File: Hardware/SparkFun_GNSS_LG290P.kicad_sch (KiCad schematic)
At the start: 59 parts, among them J1 USB_C_Receptacle, J10 Conn_01x06, J2 Conn_01x06, J3 SMA_Edge, J4 Qwiic_RA, J5 SMA_Edge, J6 Conn_01x09, J7 Qwiic_RA, J8 JST_Locking_4, J9 I2C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

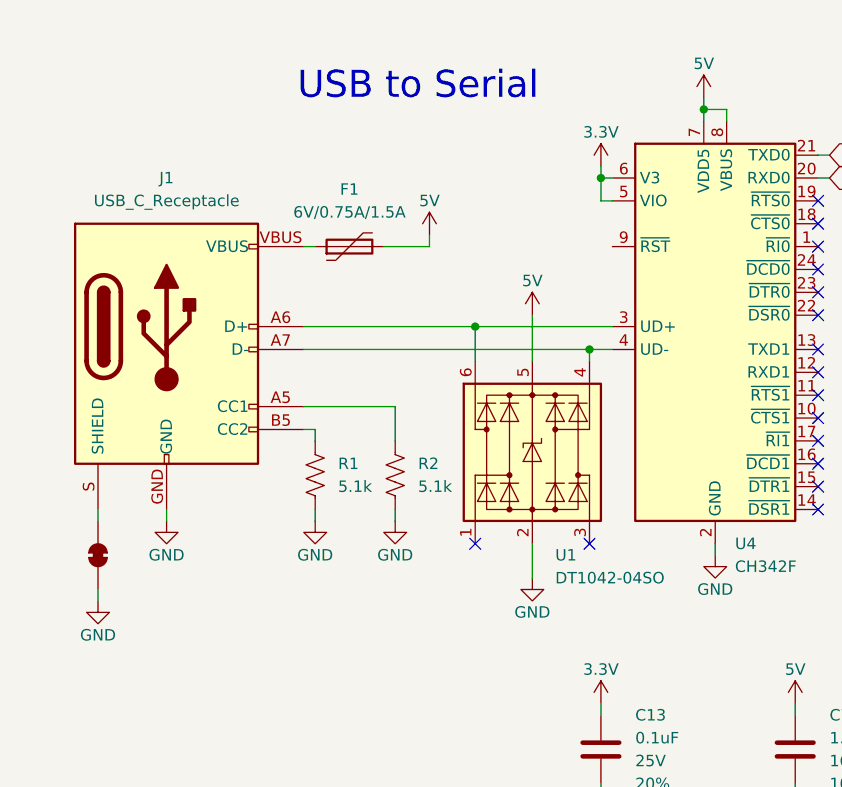
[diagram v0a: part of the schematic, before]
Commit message: Connect CH342 V3 to decoupling cap
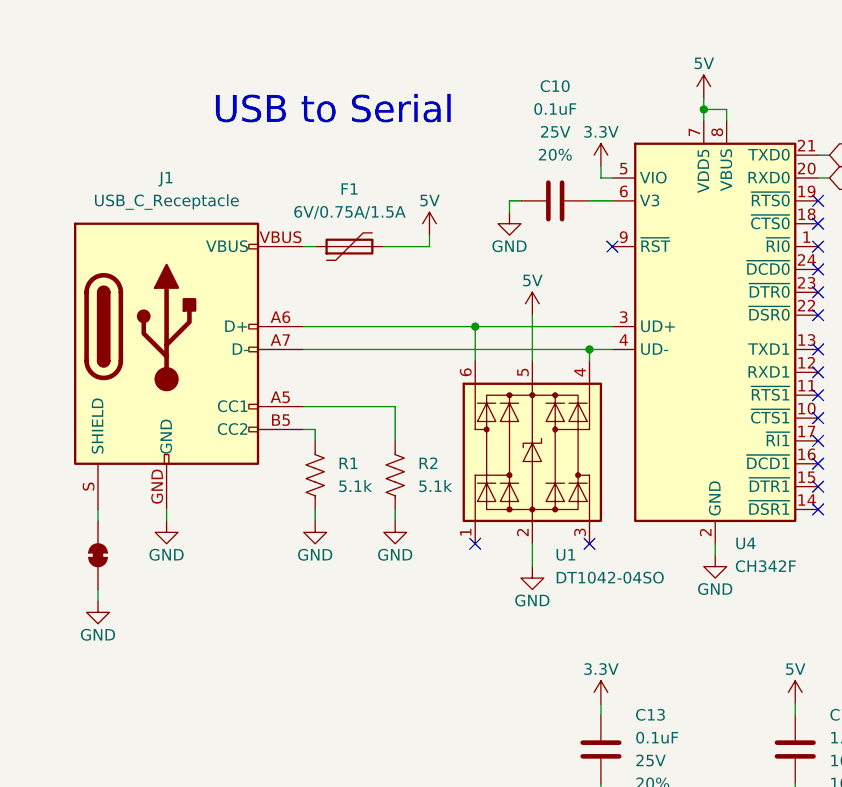
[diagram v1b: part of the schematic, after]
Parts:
- added C10: 0.1uF, SparkFun-Capacitor:C_0603_1608Metric, symbol SparkFun-Capacitor:0.1uF_0603_25V_20%
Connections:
- net 3.3V: no longer U4.6 (V3)
- net GND: now also C10.1
- net at J4.NC1 (NC): no longer J4.NC2 (NC)
- net at J1.NC2 (NC): no longer J1.NC3 (NC)
- net at J7.NC1 (NC): no longer J7.NC2 (NC)
- new net: C10.2, U4.6 (V3)
- now unconnected: U3.1 (NC), U3.17 (NC), U3.2 (NC), U3.5 (NC)
- no-connect marks 19 -> 20

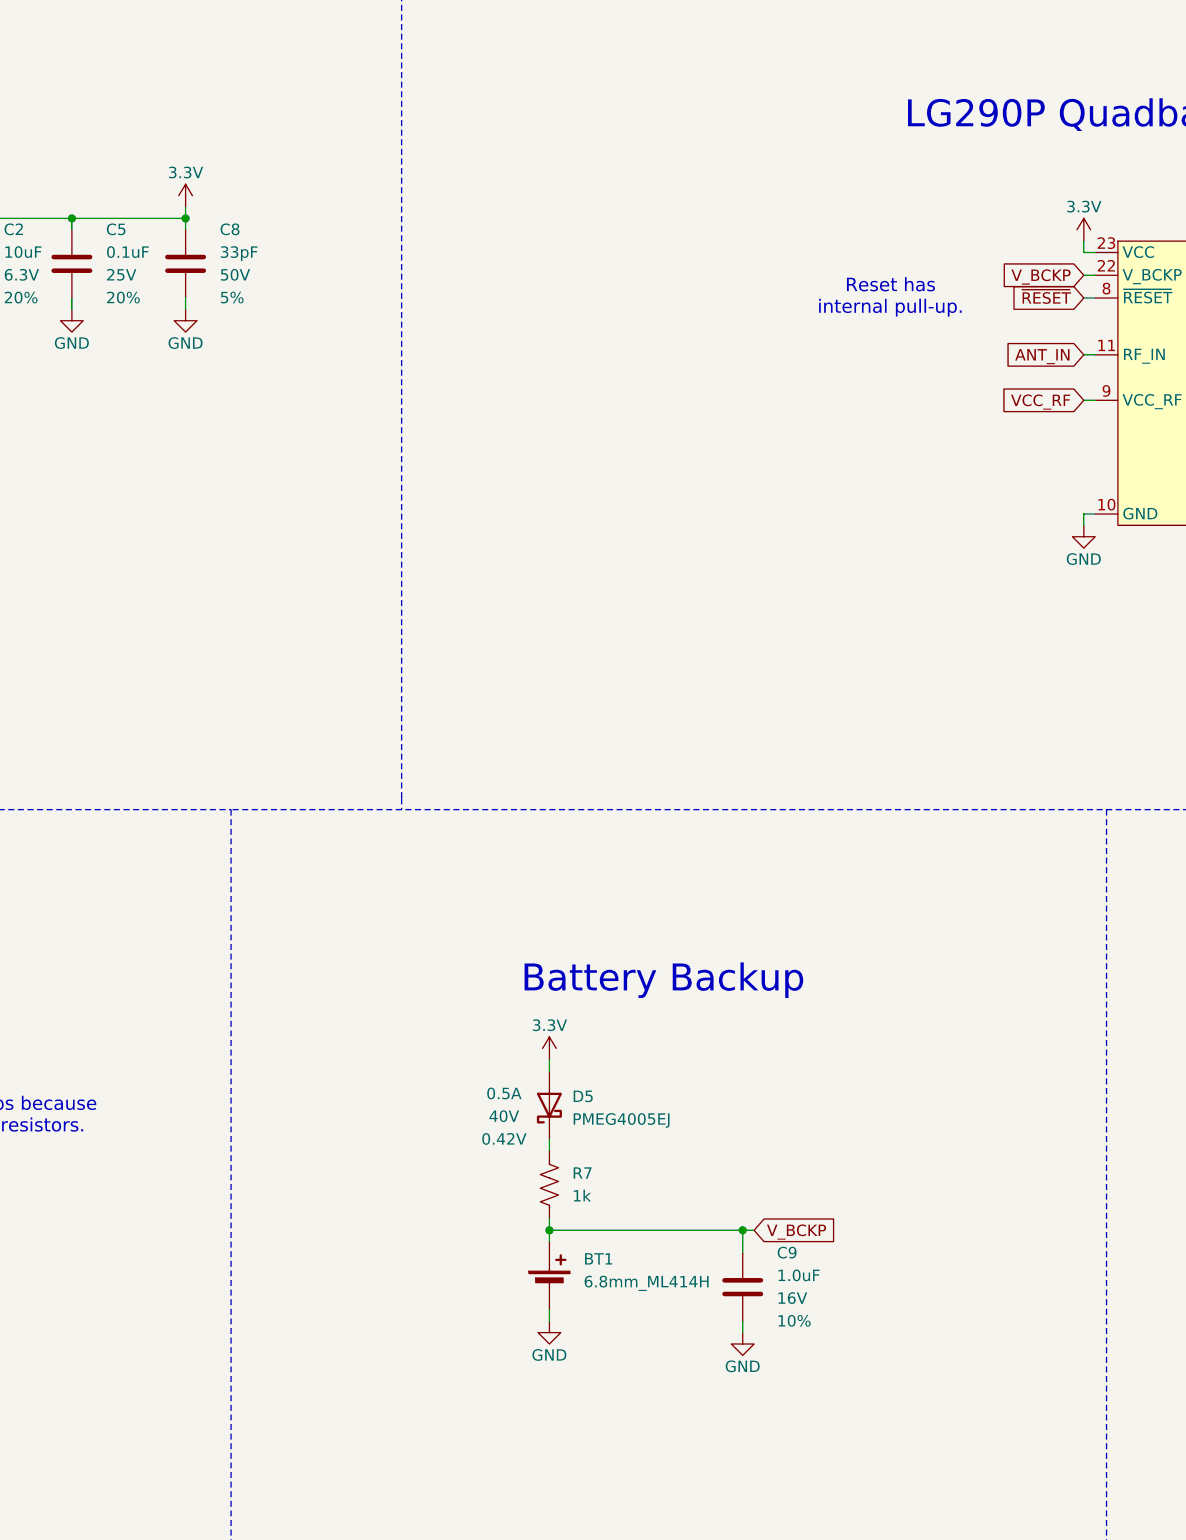
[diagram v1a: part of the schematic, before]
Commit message: Add TVS to 3V3 and VBATT. Add protocol spec.
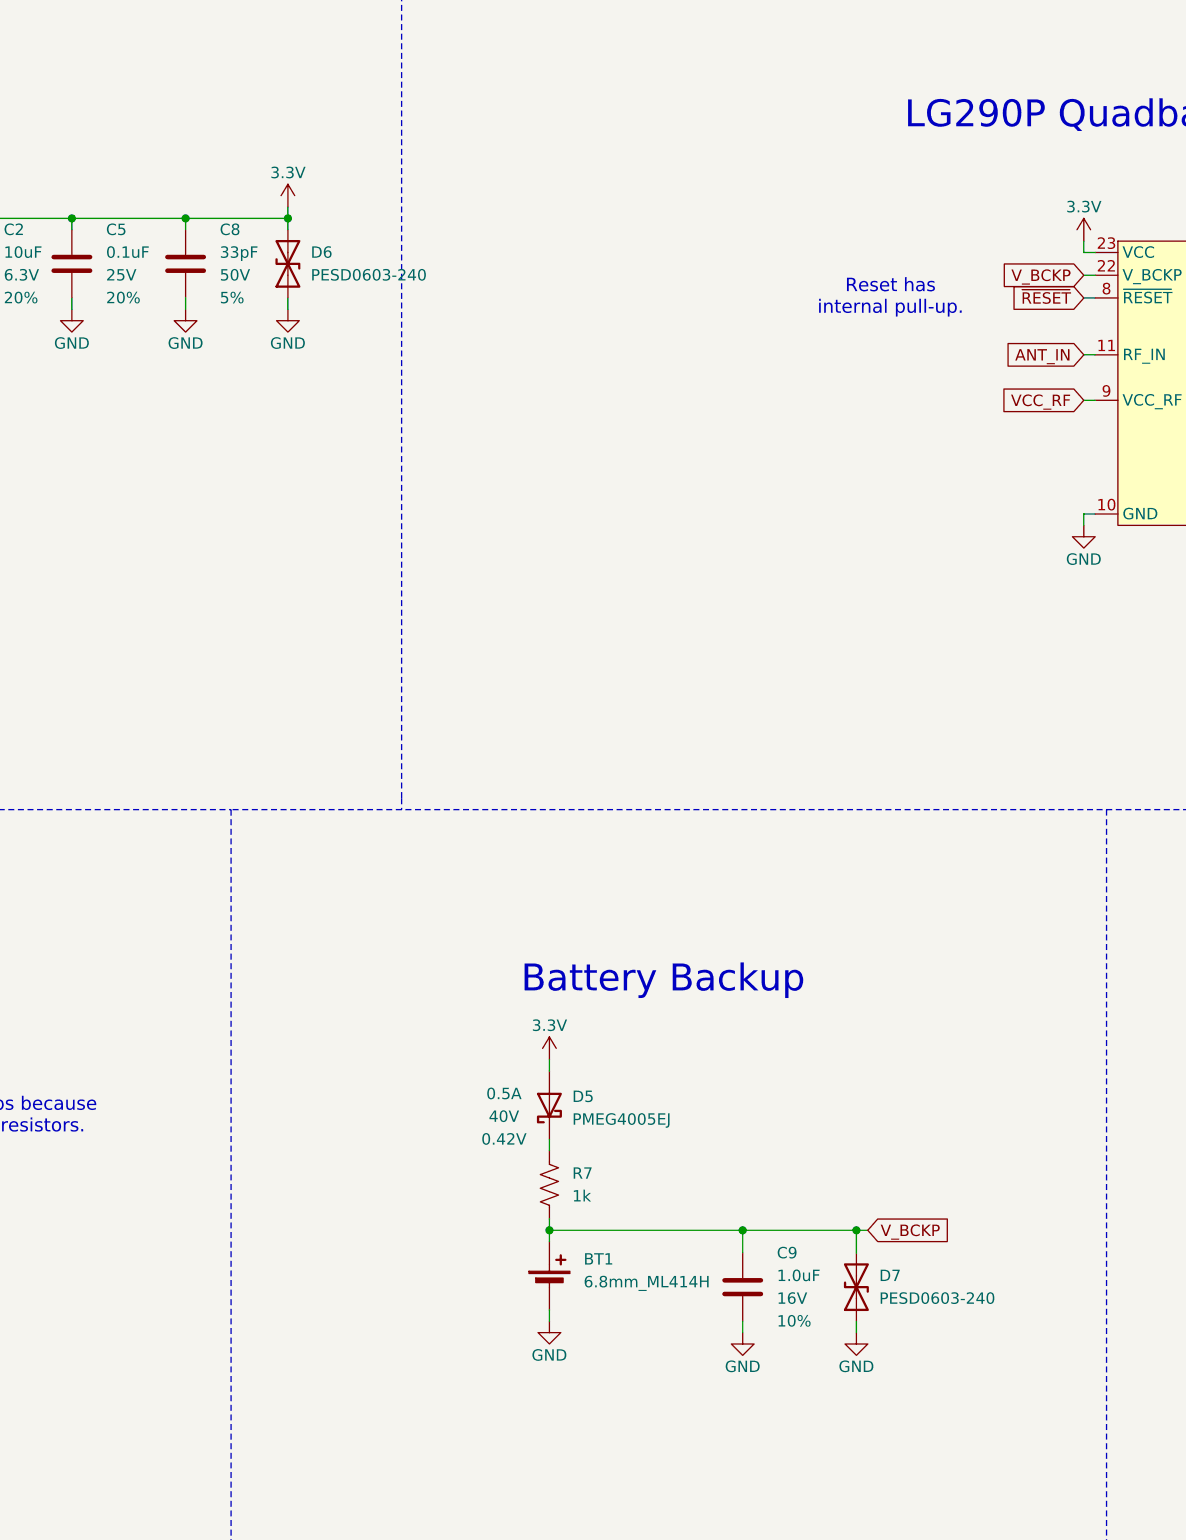
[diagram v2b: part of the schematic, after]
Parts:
- added D6, D7: PESD0603-240, SparkFun-Capacitor:C_0603_1608Metric, symbol SparkFun-DiscreteSemi:D_TVS_0603
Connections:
- net 3.3V: now also D6.2 (A2)
- net GND: now also D6.1 (A1), D7.1 (A1)
- net V_BCKP: now also D7.2 (A2)

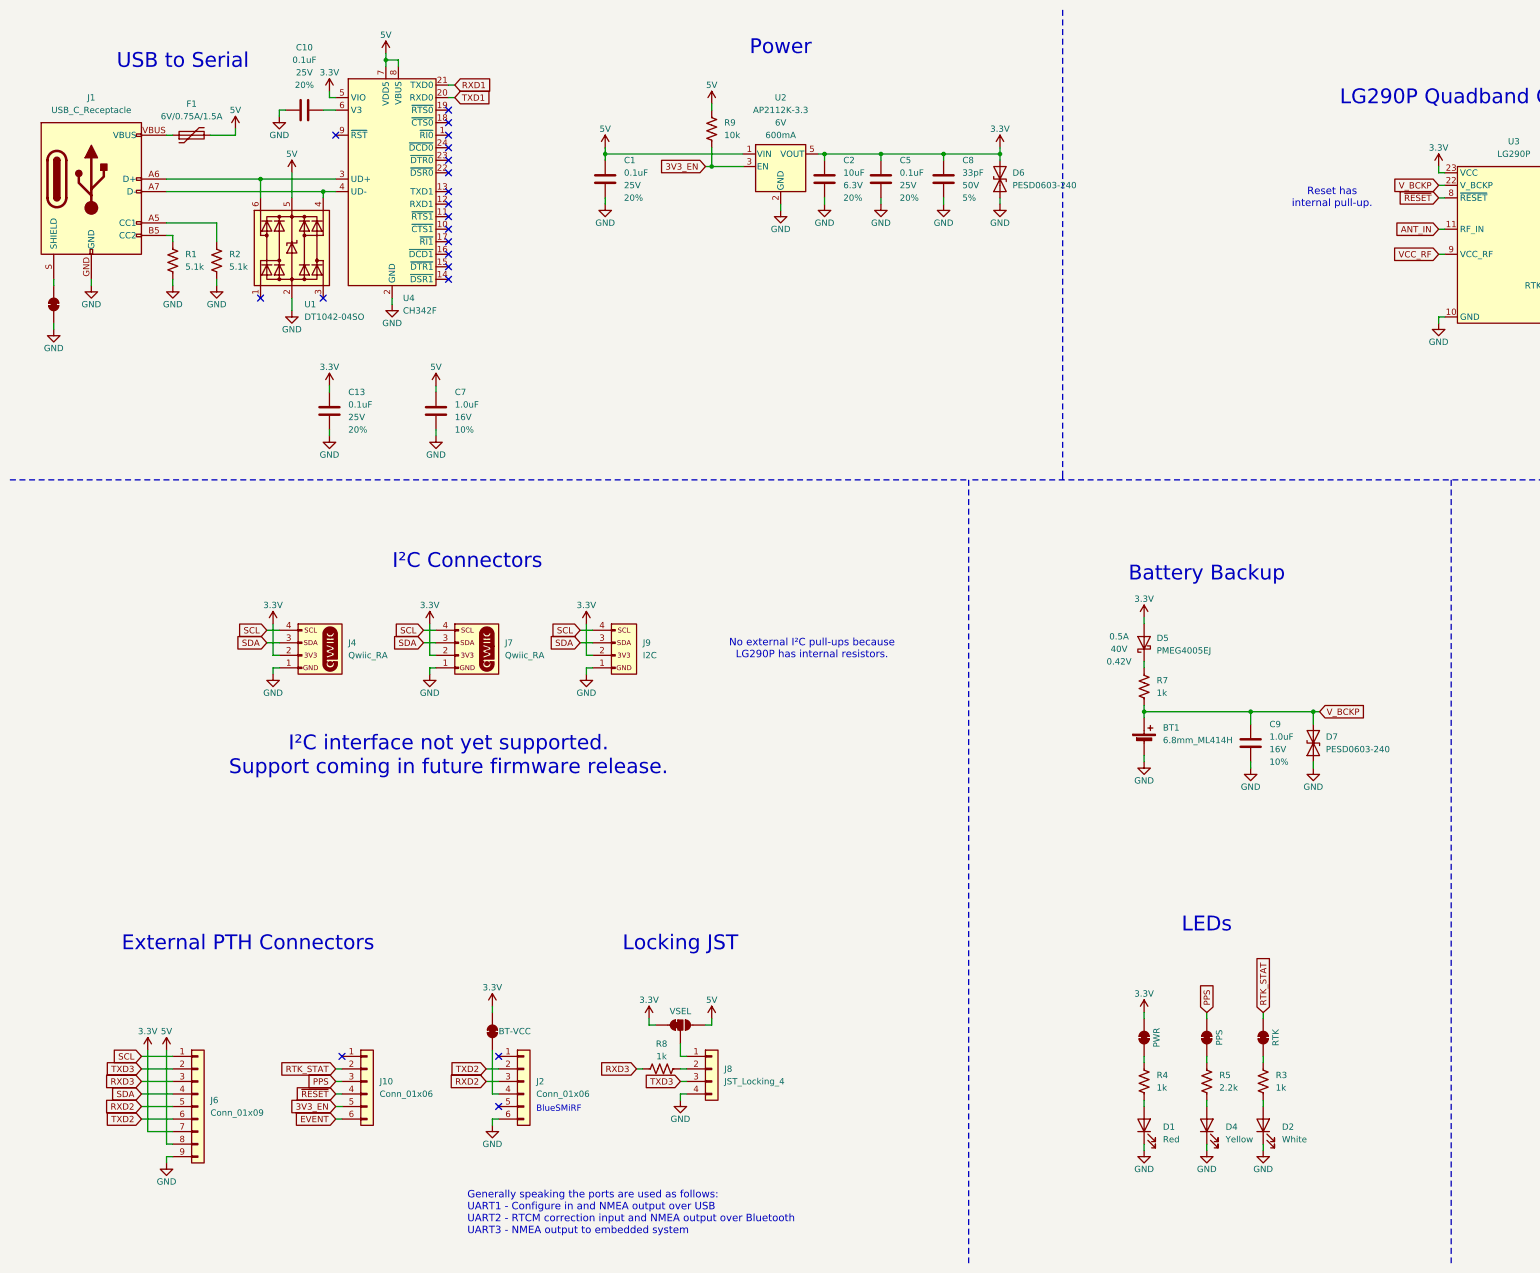
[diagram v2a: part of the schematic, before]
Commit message: Make post design review changes. Add panel files.
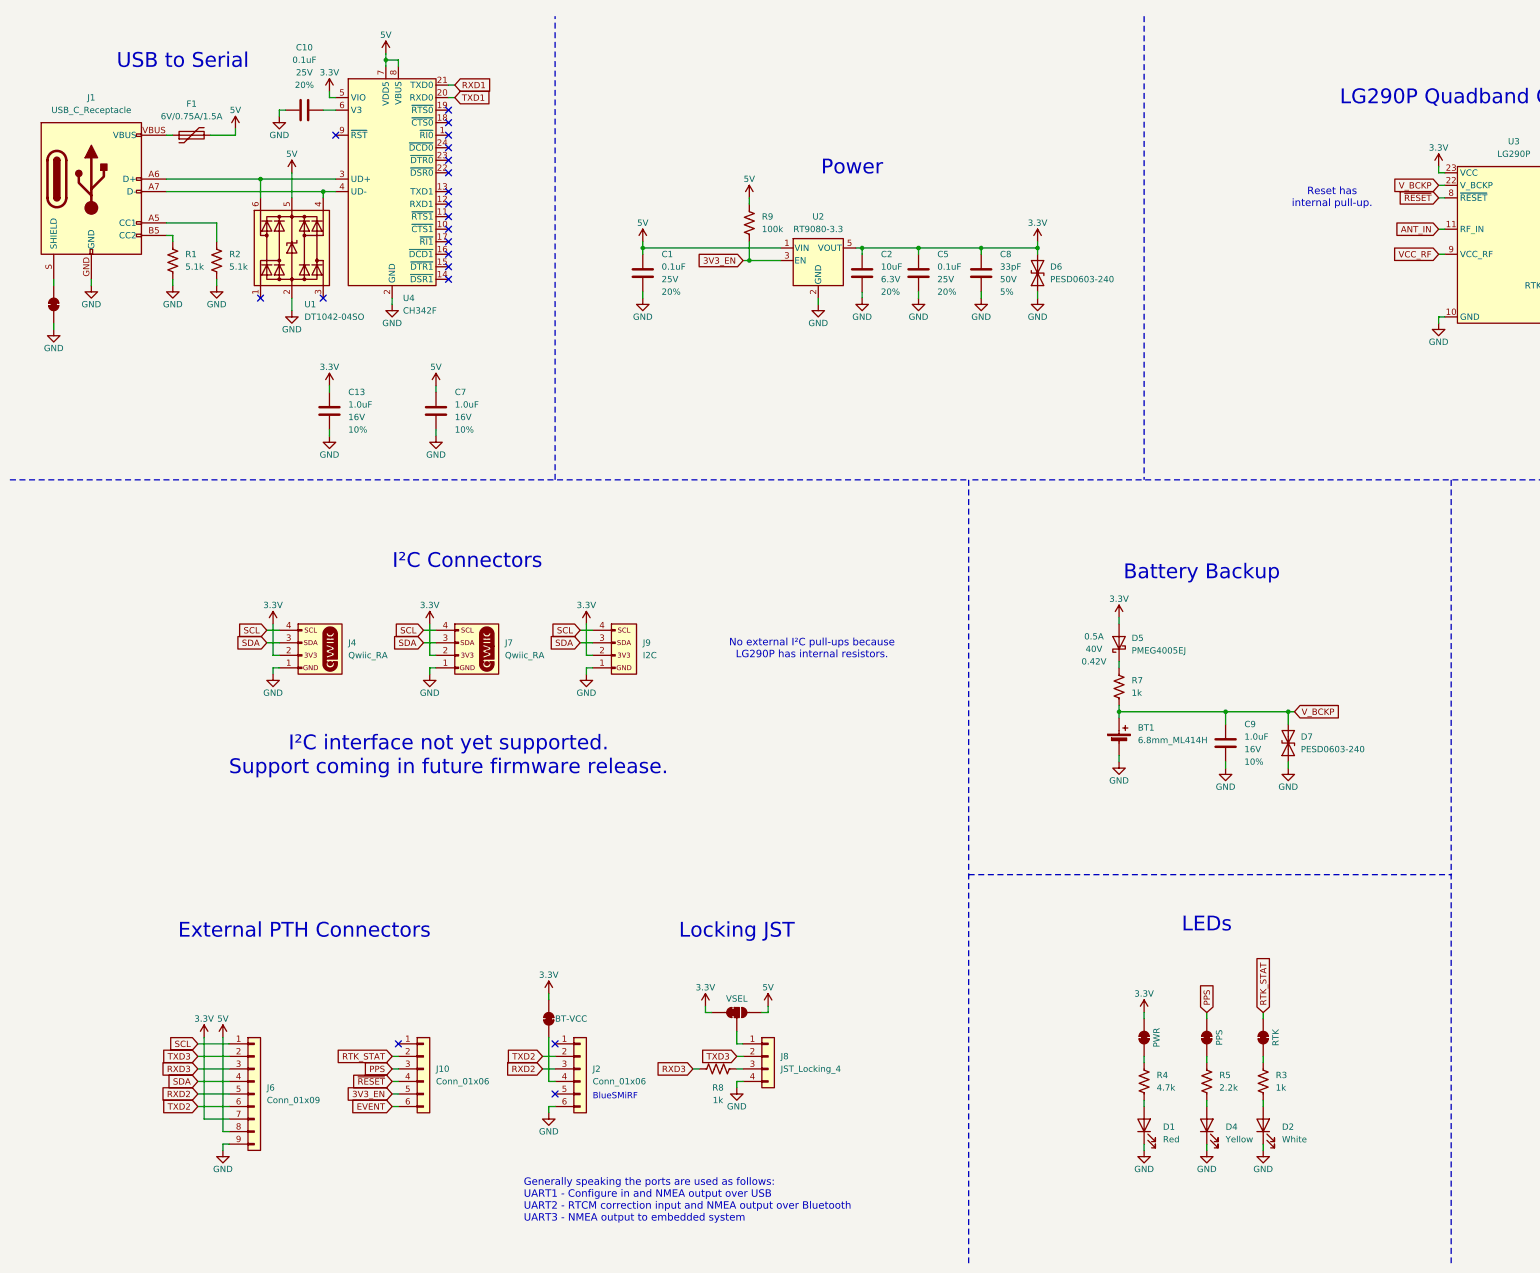
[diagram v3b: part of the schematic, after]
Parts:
- C13: value 0.1uF -> 1.0uF; symbol SparkFun-Capacitor:0.1uF_0603_25V_20% -> SparkFun-Capacitor:1.0uF_0603_16V_10%; PROD_ID CAP-00810 -> CAP-13930; Tolerance 20% -> 10%; Voltage 25V -> 16V
- R4: value 1k -> 4.7k; symbol SparkFun-Resistor:1k_0603 -> SparkFun-Resistor:4.7k_0603; PROD_ID RES-07856 -> RES-07857
- R9: value 10k -> 100k; symbol SparkFun-Resistor:10k_0603 -> SparkFun-Resistor:100k_0603; PROD_ID RES-00824 -> RES-07828
- U2: value AP2112K-3.3 -> RT9080-3.3; symbol SparkFun-Regulator:AP2112K-3.3 -> SparkFun-Regulator:RT9080-3.3; Iq 55µA -> 4µA; PROD_ID VREG-12457 -> VREG-19034
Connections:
- net TXD3: now also J8.2 (Pin_2); no longer J8.3 (Pin_3)
- net at R8.2: now also J8.3 (Pin_3); no longer J8.2 (Pin_2)
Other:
- moved on the sheet: BT1, C1, C2, C5, C8, C9, D5, D6, D7, J10, J2, J6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
